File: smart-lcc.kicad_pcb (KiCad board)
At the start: 4 copper layers, 53.2 x 53.2 mm, 116 parts, among them J1 280372-1, J2 F0503-ZV-24-20T-R, J3 Conn_01x24, J4 BM04B-SRSS-TB(LF)(SN), J5 BM04B-SRSS-TB(LF)(SN), J6 Micro_SD_Card_Det2, J7 Conn_01x12, J8 BM04B-SRSS-TB(LF)(SN), Q1 2N7002, Q2 2N7002, Q3 2N7002, Q4 2N7002, Q5 2N7002, SW1 SW_Push, SW2 SW_Push, U1 LM5050-1, U2 RP2040, U3 ESP32-S3-WROOM-1, U4 W25Q16JVSNIQ (Program Flash), U5 W25Q16JVSNIQ (Opt. Settings f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, U6 TPS82130, U7 74LVC1G125, U8 LM5050-1, Y1 XYDBPCNANF-12MHZ

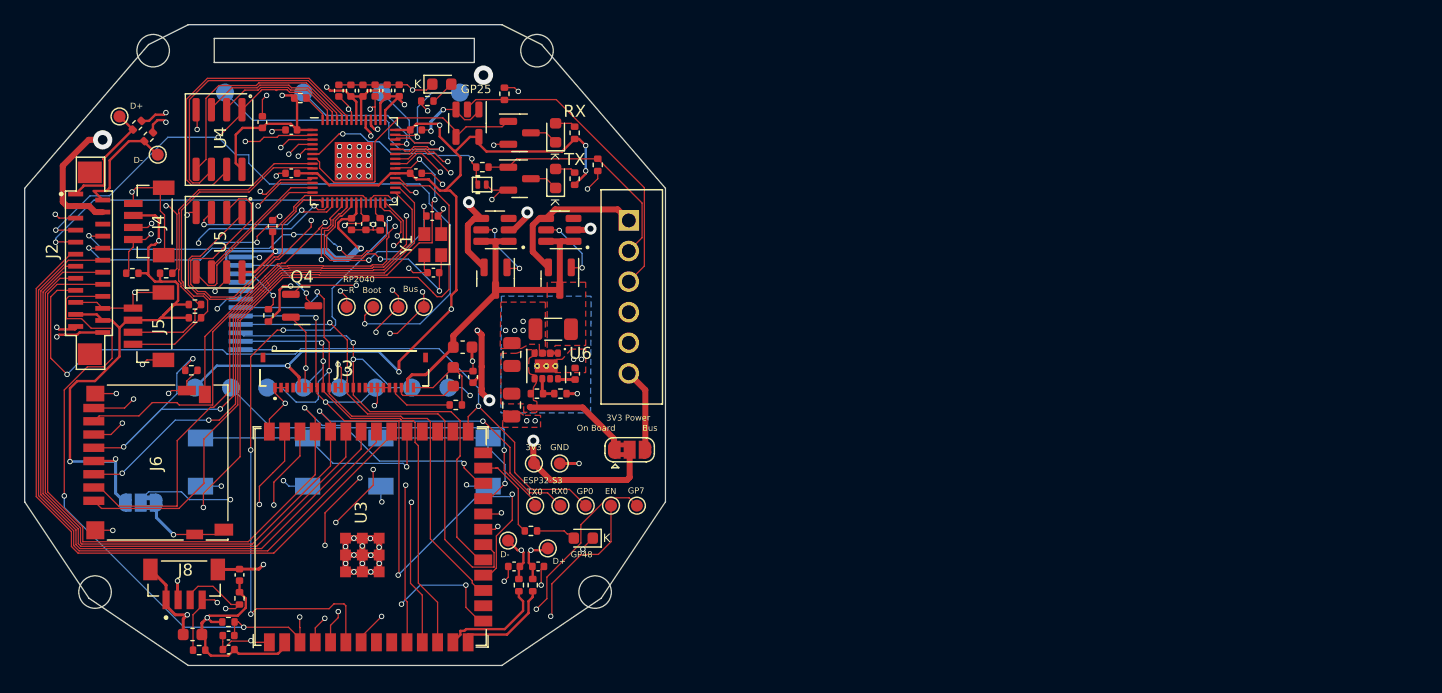
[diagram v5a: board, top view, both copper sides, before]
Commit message: Updated design for easier manufacturability
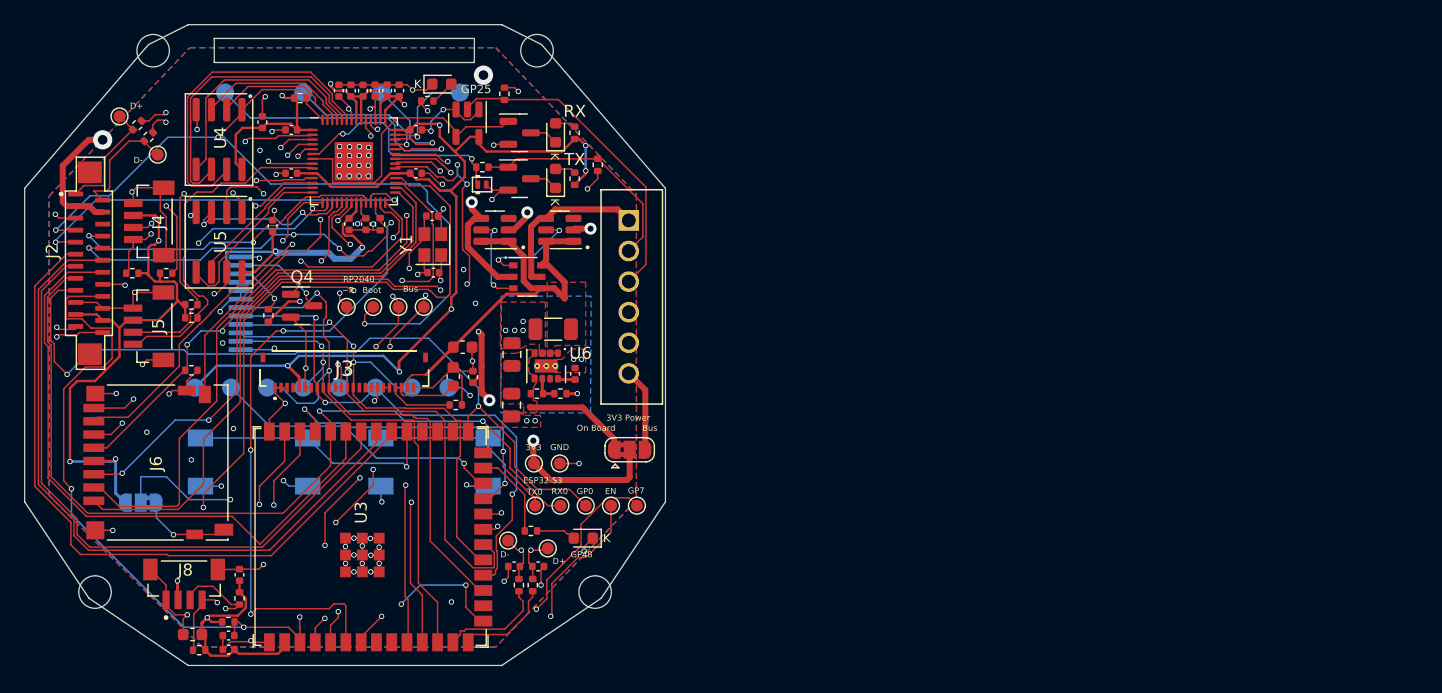
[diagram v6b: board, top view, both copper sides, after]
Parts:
- removed Q3, Q5: 2N7002, Package_TO_SOT_SMD:SOT-23
- added Q6: NTGD3148NT1G, Package_SO:TSOP-6_1.65x3.05mm_P0.95mm, F.Cu at (64.6, 43.8)
- moved R13 0.30 mm to (36.7, 47.2)
- moved R15 0.30 mm to (36.7, 46.1)
- moved C16 0.20 mm to (49.8, 39.4)
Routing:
- net ESP32_TXD0: track 78.9 -> 48.2 mm, vias 2 -> 3
- net RP2040_SET_MISO: track 28.8 -> 15.3 mm, vias 0 -> 2
- net RP2040_SD_SCLK: track 53.0 -> 39.7 mm, vias 3 -> 2
- net SSD1309_CS: track 58.1 -> 45.1 mm, vias 4 -> 3
- net RP2040_SET_CS: track 34.3 -> 24.2 mm
- net RP2040_SD_DAT2: track 53.7 -> 63.5 mm, vias 2 -> 4
- net ESP32_RXD0: track 77.9 -> 73.2 mm
- net RP2040_SD_MISO_DAT0: track 42.3 -> 46.3 mm
- net Net-(U2-XIN): track 19.3 -> 15.5 mm
- net VIN: track 30.5 -> 34.0 mm
- net +3V3: track 294.2 -> 291.4 mm
- net Net-(Q6A-G): track 5.91 -> 8.60 mm
- net VIN_DEBUG: track 63.4 -> 65.7 mm
- net ESP32_TMS: track 55.2 -> 53.1 mm
- net Net-(JP1-C): track 38.4 -> 40.6 mm
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- added copper zone on In2.Cu, net GND
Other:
- board text added: "github.com/open-lcc/open-lcc-board"
- board text removed: "github.com/magnusnordlander/open-lcc"

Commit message: Added revision R2C
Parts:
- added R26: 18K, Resistor_SMD:R_0402_1005Metric, F.Cu at (69.0, 37.2)
- added R27: 18K, Resistor_SMD:R_0402_1005Metric, F.Cu at (60.8, 43.8)
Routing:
- net 12V_OLED: track 14.1 -> 15.1 mm
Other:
- board text added: "Rev R2C"
- board text removed: "Rev R2B"
